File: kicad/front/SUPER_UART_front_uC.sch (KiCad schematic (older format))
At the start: 44 parts, among them Q1 PDTA143ZT, SW1 5V, SW10 TX, SW11 ISO, SW12 I2C, SW13 SPI, SW14 I2C, SW15 SPI, SW18 SPY, SW19 BOOT, SW2 3V3, SW3 2V5, SW4 1V8, SW5 5V, SW6 3V3, SW7 2V5, SW8 1V8, SW9 RX, U11 STM32F030C6T6

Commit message: Working on schematic
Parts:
- added C37, C51: 27p, 0603_N, symbol C
- added C? (x4): 100n, 0603_N, symbol C
- added Q4: 12MHz, XT3.2x2.5_N, symbol XT_3.2x2.5
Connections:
- net labels added: +3V3, 1V8_LED_A, 1V8_SEL_A, 2V5_LED_A, 2V5_SEL_A, 3V3_LED_A, 3V3_SEL_A, 5V_LED_A, 5V_SEL_A, I2C_LED_A, I2C_SEL_A, ISO_SEL, LED, RXD_D3, RX_LED, RX_SEL, SPI_LED_A, SPI_SEL_A, SPY_LED_A, SPY_SEL_A, TR_LED, TR_SEL, TXD_D
- net labels removed: 1V8_LED_ISO, 1V8_SEL_ISO, 2V5_LED_ISO, 2V5_SEL_ISO, 3V3_LED_ISO, 3V3_SEL_ISO, 5V_LED_ISO, 5V_SEL_ISO, FT_RXD_A, FT_TXD_A, I2C_LED_ISO, I2C_SEL_ISO, ISO_3V3, ISO_GND, ISO_LED_ISO, ISO_SEL_ISO, RX_LED_ISO, RX_SEL_ISO, SPI_LED_ISO, SPI_SEL_ISO, SPY_LED, SPY_SEL, TR_LED_ISO, TR_SEL_ISO
- wire segments 118 -> 153
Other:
- note added: "TIM3_CH1"
- note added: "TIM3_CH2"
- note added: "TIM3_CH3"
- note added: "TIM3_CH4"
- note added: "USART1_RX"
- note added: "USART1_TX"
- moved on the sheet: C19, C20, D33, D34, D35, D36, D37, D38, D39, D40, D41, D42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

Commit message: Working on schematic
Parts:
- removed C37, C51: 27p, 0603_N, symbol C
- removed Q4: 12MHz, XT3.2x2.5_N, symbol XT_3.2x2.5
- removed TP1: 3V3, pnConnector:TP_1mm, symbol Testpoint
- removed TP2: SWDIO, pnConnector:TP_1mm, symbol Testpoint
- removed TP3: SWDCLK, pnConnector:TP_1mm, symbol Testpoint
- removed TP4: RST, pnConnector:TP_1mm, symbol Testpoint
- removed TP5: GND, pnConnector:TP_1mm, symbol Testpoint
- added C10, C9: 1u, 0603_N, symbol C
- added C11, C8: 10u, niceRLC:0805_N, symbol C
- added CON2: PIN-2x3, pnPinheaders:PIN3x2SMD, symbol PIN-2x3
- added LED17: EN_A, pnSemiconductor:LED_3.2x2, symbol diode_LED
- added LED18: EN_B, pnSemiconductor:LED_3.2x2, symbol diode_LED
- added LED19: EN_C, pnSemiconductor:LED_3.2x2, symbol diode_LED
- added LED20: EN_D, pnSemiconductor:LED_3.2x2, symbol diode_LED
- added R1: R, pnRLC:0805_JUMPER, symbol R
- added RN1: R, pnRLC:4x0603_N, symbol R_network_4
- added RN2: N.C., pnRLC:4x0603_N, symbol R_network_4
- added U2: MIC5504-3.3YM5-TR, niceSemiconductors:SOT23-5_N, symbol MIC5504-3.3YM5-TR
- added U3: AP7333-33SAG-7, SOT23-3_N, symbol AP7333-33SAG-7
- LED1: renamed from D37; value 5V -> 5V_1
- LED10: renamed from D34; value 3V3 -> 3V3_2
- LED11: renamed from D35; value 2V5 -> 2V5_2
- LED12: renamed from D36; value 1V8 -> 1V8_2
- LED13: renamed from D44; value I2C -> I2C_A
- LED14: renamed from D45; value SPI -> SPI_A
- LED15: renamed from D46; value I2C -> I2C_B
- LED16: renamed from D47; value SPI -> SPI_B
- LED2: renamed from D38; value 3V3 -> 3V3_1
- LED3: renamed from D39; value 2V5 -> 2V5_1
- LED4: renamed from D40; value 1V8 -> 1V8_1
- LED9: renamed from D33; value 5V -> 5V_2
- SW1: value 5V -> 5V_1
- SW10: renamed from SW6; value 3V3 -> 3V3_2
- SW11: renamed from SW7; value 2V5 -> 2V5_2
- SW12: renamed from SW8; value 1V8 -> 1V8_2
- SW13: renamed from SW14; value I2C -> I2C_A
- SW14: renamed from SW15; value SPI -> SPI_A
- SW15: renamed from SW12; value I2C -> I2C_B
- SW16: renamed from SW13; value SPI -> SPI_B
- SW2: value 3V3 -> 3V3_1
- SW3: value 2V5 -> 2V5_1
- SW4: value 1V8 -> 1V8_1
- SW9: renamed from SW5; value 5V -> 5V_2
- gave numbers to parts that had none: 4
- renumbered C19 to C6, C20 to C7, D51 to D1, D41 to LED5, D42 to LED6, D50 to LED7, D43 to LED8, R3 to R2, SW19 to SW17, SW9 to SW5, SW10 to SW6, SW18 to SW7, SW11 to SW8, U11 to U1
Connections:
- net labels added: +5V, CLPD_OE, COL1, COL2, COL3, COL4, CPLD_BOOT_EN, FTDI_RESET, I2C_PU_EN_A, I2C_PU_EN_B, LED1, LED1uC, LED2, LED2uC, LED3, LED3uC, LED4, LED4uC, LED5, LED5uC, SPI_EN_A, SPI_EN_B, SR_CLK, SR_DATA, SR_LOAD, SW1, SW2, SW3, SW4, VDD1_SEL1, VDD1_SEL2, VDD1_SEL3, VDD2_SEL1, VDD2_SEL2, VDD2_SEL3, ~PWREN, ~USB_SUSPEND, ~VDD1_EN, ~VDD1_ERR, ~VDD2_EN, ~VDD2_ERR
- net labels removed: 1V8_LED, 1V8_LED_A, 1V8_SEL, 1V8_SEL_A, 2V5_LED, 2V5_LED_A, 2V5_SEL, 2V5_SEL_A, 3V3_LED, 3V3_LED_A, 3V3_SEL, 3V3_SEL_A, 5V_LED, 5V_LED_A, 5V_SEL, 5V_SEL_A, I2C_LED, I2C_LED_A, I2C_SEL, I2C_SEL_A, ISO_SEL, LED, RX_LED, RX_SEL, SPI_LED, SPI_LED_A, SPI_SEL, SPI_SEL_A, SPY_LED_A, SPY_SEL_A, TR_LED, TR_SEL
- wire segments 153 -> 269
- no-connect marks 0 -> 1
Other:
- note added: "SPI1_MISO"
- note added: "SPI1_MOSI"
- note added: "SPI1_NSS"
- note added: "SPI1_SCK"
- note added: "TIM1_CH1"
- moved on the sheet: C6, C7, D1, LED1, LED10, LED11, LED12, LED13, LED14, LED15, LED16, LED2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

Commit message: Working on schematic
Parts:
- added TP1, TP10, TP11, TP12, TP13, TP14, TP15, TP16, TP17, TP18, TP19, TP2, TP20, TP21, TP22, TP23, TP24, TP25, TP26, TP27, TP28, TP29, TP3, TP30, TP31, TP32, TP33, TP34, TP35, TP4, TP5, TP6, TP7, TP8, TP9: Testpoint, pnConnector:TP_1mm, symbol Testpoint
- LED1, LED10, LED11, LED12, LED13, LED14, LED15, LED16, LED17, LED18, LED19, LED2, LED20, LED3, LED4, LED5, LED6, LED7, LED8, LED9: footprint pnSemiconductor:LED_3.2x2 -> pnSemiconductor:0805D
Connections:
- net labels added: VDD1, VDD2
- wire segments 269 -> 278

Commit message: PCB placement
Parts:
- removed U3: AP7333-33SAG-7, SOT23-3_N, symbol AP7333-33SAG-7
- R1: footprint pnRLC:0805_JUMPER -> niceRLC:0603_R_N; Fieldname (none) -> Value
- RN1, RN2: footprint pnRLC:4x0603_N -> niceRLC:4x0603_N
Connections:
- wire segments 278 -> 274
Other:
- moved on the sheet: C10, C11, C8, C9

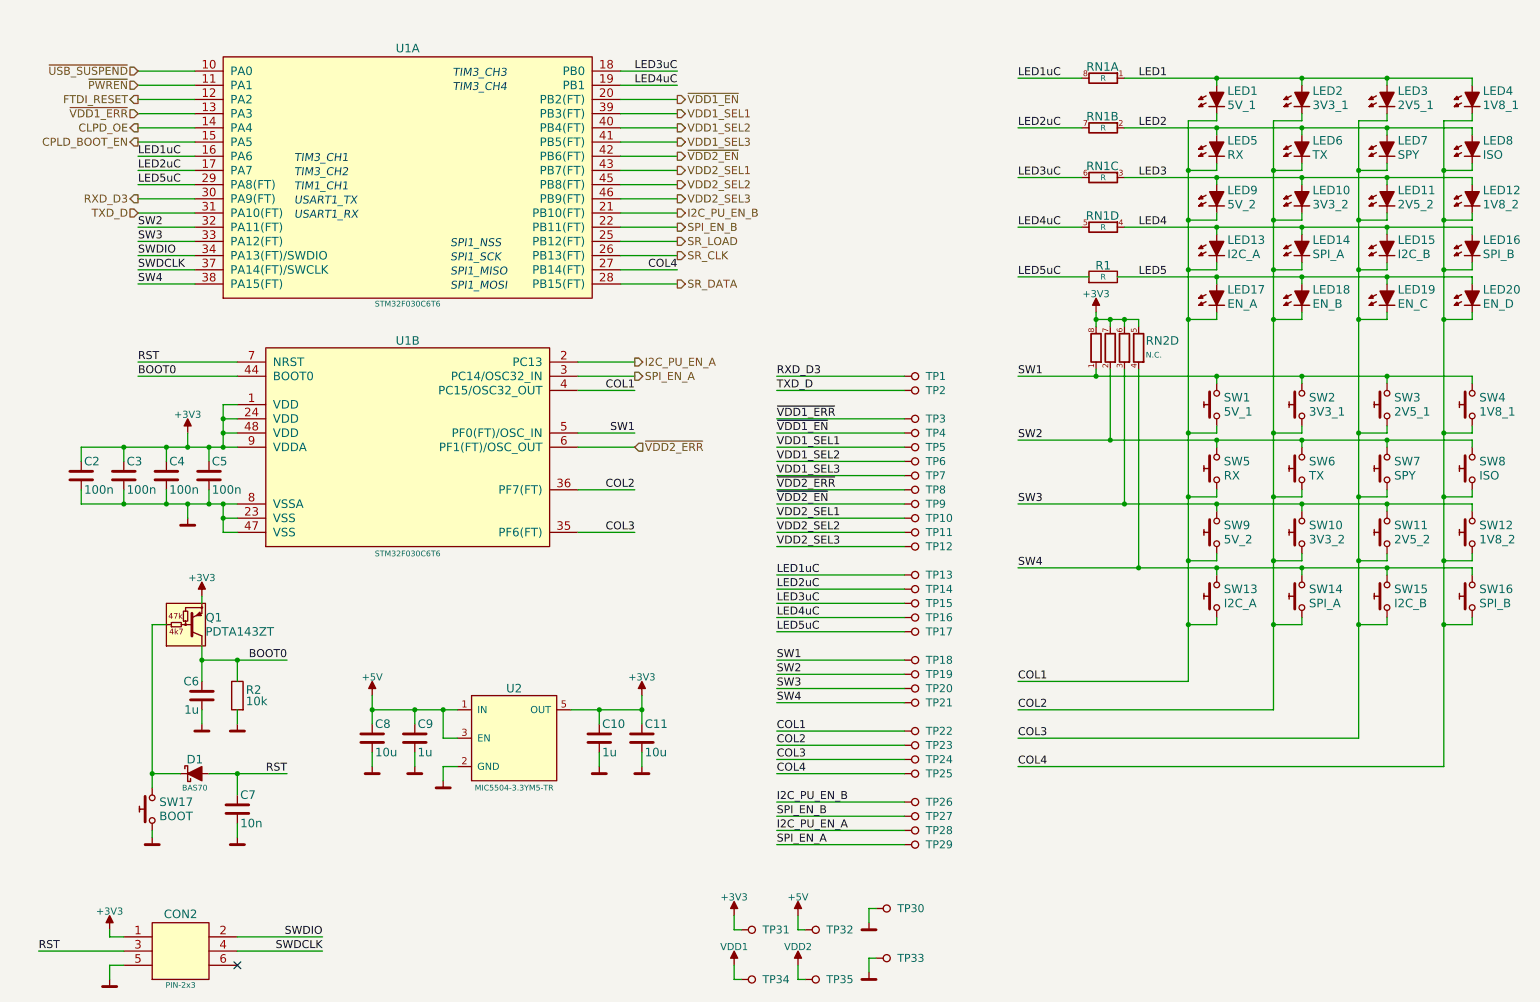
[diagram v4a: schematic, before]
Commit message: Routing before moving to 4 layers
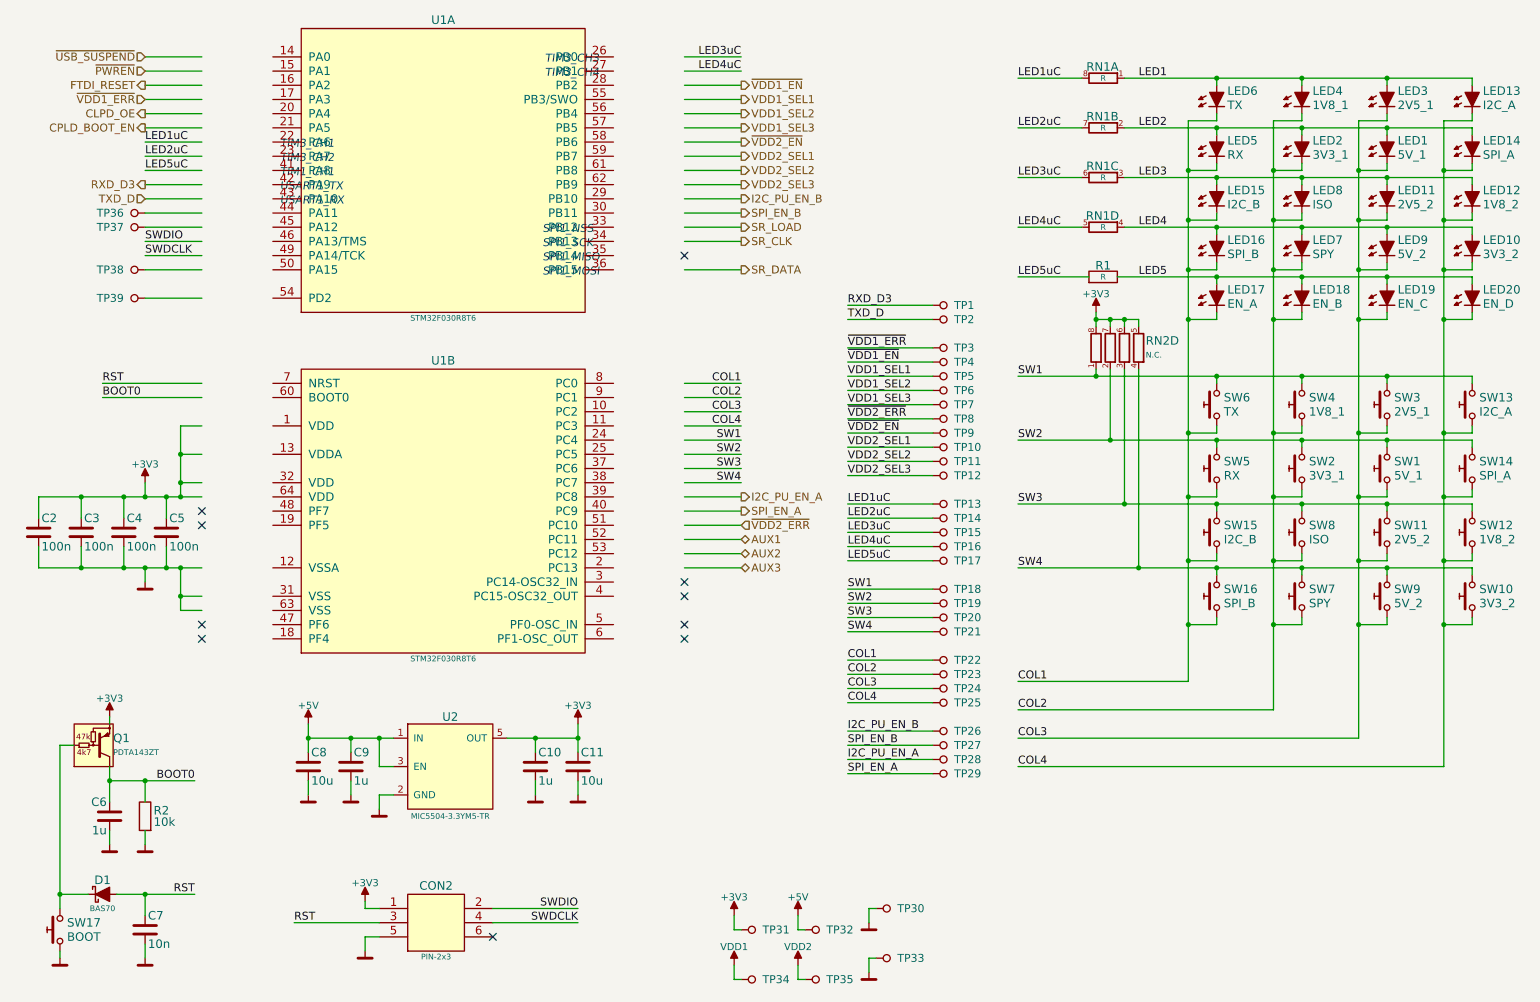
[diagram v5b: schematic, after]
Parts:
- removed U1: STM32F030C6T6, ST_LQFP48_ST_default, symbol STM32F030C6T6
- added TP36, TP37, TP38, TP39: Testpoint, pnConnector:TP_1mm, symbol Testpoint
- added U1: STM32F030R8T6, niceSemiconductors:QFP-64-0.5_N, symbol STM32F030R8T6
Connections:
- net labels added: AUX1, AUX2, AUX3
- wire segments 274 -> 281
- no-connect marks 1 -> 10
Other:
- moved on the sheet: C10, C11, C2, C3, C4, C5, C6, C7, C8, C9, CON2, D1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

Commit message: Front board routed
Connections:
- wire segments 281 -> 288
- no-connect marks 10 -> 4
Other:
- moved on the sheet: C2, C3, C4, C5, TP36, TP37

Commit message: Add missing files
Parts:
- removed TP30, TP31, TP32, TP33, TP34, TP35: Testpoint, pnConnector:TP_1mm, symbol Testpoint
- R1, RN1: value R -> 220R
- RN1: value R -> 220R; Fieldname (none) -> Value
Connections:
- net labels added: CPLD_OE, ~I2C_PU_EN_A, ~I2C_PU_EN_B
- net labels removed: CLPD_OE, VDD1, VDD2
- wire segments 288 -> 267
- no-connect marks 4 -> 10
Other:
- moved on the sheet: C10, C11, C2, C3, C4, C5, C6, C7, C8, C9, CON2, D1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
